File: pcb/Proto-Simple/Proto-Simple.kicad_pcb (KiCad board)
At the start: 2 copper layers, 52 x 63 mm, 339 parts, among them J1 Conn_01x04, J10 Conn_01x01, J11 Conn_01x01, J12 Conn_01x01, J13 Conn_01x01, J14 Conn_01x01, J2 Conn_01x01, J3 Conn_01x01, J4 Conn_01x01, J41 Conn_01x01, J42 Conn_01x01, J43 Conn_01x01, J44 Conn_01x01, J45 Conn_01x01, J46 Conn_01x01, J47 Conn_01x01, J5 Conn_01x01, J6 Conn_01x01, J7 Conn_01x01, J8 Conn_01x01, J9 Conn_01x01, SW100 SW_DPDT_x2, SW101 SW_DPDT_x2

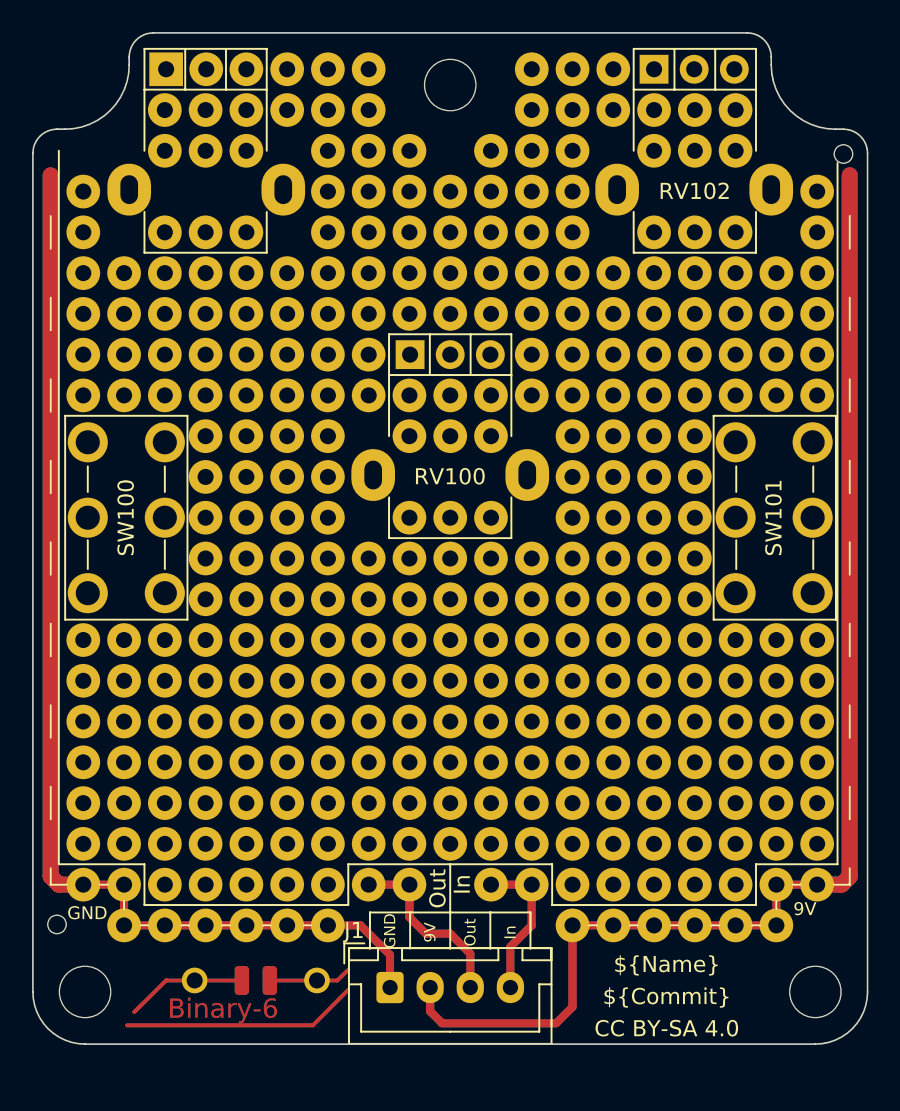
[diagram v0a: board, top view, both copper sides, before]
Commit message: [ProtoSimple] Recreate PCB according to new base template
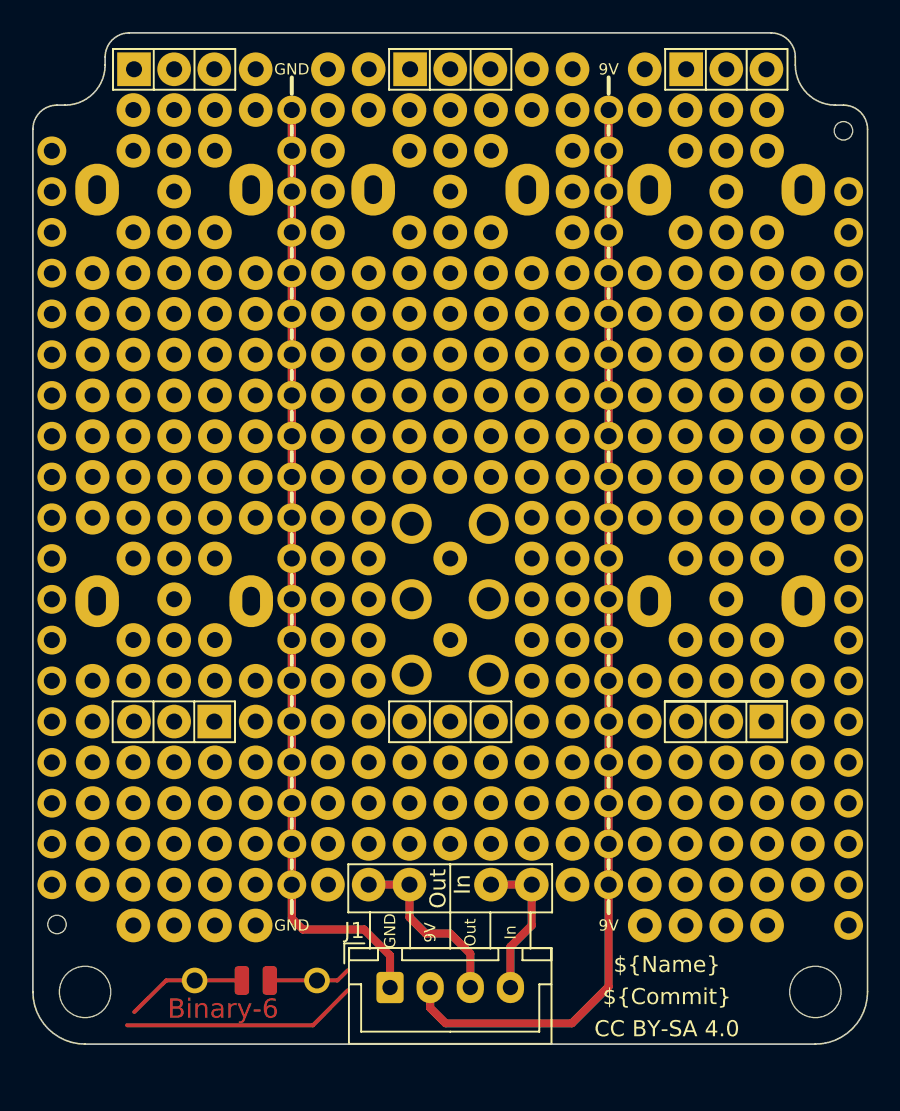
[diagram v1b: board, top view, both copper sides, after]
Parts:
- removed the MK2 at (149.5, 70.8)
- removed the REF** at (162.2, 118.0)
- removed the REF** at (126.6, 87.5)
- removed the REF** at (169.8, 87.5)
- removed the REF** at (134.3, 112.9)
- removed the REF** at (167.3, 120.6)
- removed the REF** at (126.6, 118.0)
- removed the REF** at (134.3, 120.6)
- removed the REF** at (129.2, 105.3)
- removed the REF** at (134.3, 102.8)
- removed the REF** at (149.5, 102.8)
- removed the REF** at (159.7, 120.6)
- removed the REF** at (139.3, 118.0)
- removed the REF** at (147.0, 105.3)
- removed the REF** at (126.6, 90.1)
- removed the REF** at (167.3, 79.9)
- removed the REF** at (129.2, 112.9)
- removed the REF** at (134.3, 100.2)
- removed the REF** at (136.8, 72.3)
- removed the REF** at (131.7, 90.1)
- removed the REF** at (162.2, 107.9)
- removed the REF** at (131.7, 107.9)
- removed the REF** at (164.7, 92.6)
- removed the REF** at (147.0, 97.7)
- removed the REF** at (164.7, 100.2)
- removed the REF** at (139.3, 92.6)
- removed the REF** at (164.7, 90.1)
- removed the REF** at (131.7, 74.8)
- removed the REF** at (167.3, 112.9)
- removed the REF** at (162.2, 87.5)
- removed the REF** at (126.6, 107.9)
- removed the REF** at (134.3, 118.0)
- removed the REF** at (131.7, 118.0)
- removed the REF** at (126.6, 82.5)
- removed the REF** at (172.4, 118.0)
- removed the REF** at (139.3, 85.0)
- removed the REF** at (129.2, 107.9)
- removed the REF** at (159.7, 115.5)
- removed the REF** at (129.2, 90.1)
- removed the REF** at (154.6, 79.9)
- removed the REF** at (136.8, 110.4)
- removed the REF** at (167.3, 118.0)
- removed the REF** at (164.7, 112.9)
- removed the REF** at (162.2, 100.2)
- removed the REF** at (139.3, 72.3)
- removed the REF** at (139.3, 107.9)
- removed the REF** at (164.7, 87.5)
- removed the REF** at (159.7, 69.8)
- removed the REF** at (139.3, 82.5)
- removed the REF** at (162.2, 74.8)
- removed the REF** at (134.3, 90.1)
- removed the REF** at (136.8, 107.9)
- removed the REF** at (126.6, 112.9)
- removed the REF** at (162.2, 90.1)
- removed the REF** at (162.2, 112.9)
- removed the REF** at (162.2, 72.3)
- removed the REF** at (126.6, 110.4)
- removed the REF** at (136.8, 74.8)
- removed the REF** at (159.7, 85.0)
- removed the REF** at (144.4, 74.8)
- removed the REF** at (164.7, 95.2)
- removed the REF** at (134.3, 74.8)
- removed the REF** at (126.6, 115.5)
- removed the REF** at (167.3, 82.5)
- removed the REF** at (139.3, 95.2)
- removed the REF** at (162.2, 120.6)
- removed the REF** at (172.4, 105.3)
- removed the REF** at (172.4, 85.0)
- removed the REF** at (147.0, 102.8)
- removed the REF** at (136.8, 85.0)
- removed the REF** at (159.7, 100.2)
- removed the REF** at (129.2, 87.5)
- removed the REF** at (129.2, 110.4)
- removed the REF** at (164.7, 107.9)
- removed the REF** at (154.6, 74.8)
- removed the REF** at (169.8, 107.9)
- removed the REF** at (136.8, 105.3)
- removed the REF** at (134.3, 79.9)
- removed the REF** at (164.7, 74.8)
- removed the REF** at (136.8, 120.6)
- removed the REF** at (139.3, 102.8)
- removed the REF** at (164.7, 79.9)
- removed the REF** at (134.3, 107.9)
- removed the REF** at (147.0, 100.2)
- removed the REF** at (167.3, 72.3)
- removed the REF** at (159.7, 92.6)
- removed the REF** at (129.2, 115.5)
- removed the REF** at (139.3, 100.2)
- removed the REF** at (131.7, 87.5)
- removed the REF** at (139.3, 115.5)
- removed the REF** at (134.3, 110.4)
- removed the REF** at (139.3, 90.1)
- removed the REF** at (164.7, 105.3)
- removed the REF** at (131.7, 79.9)
- removed the REF** at (159.7, 102.8)
- removed the REF** at (136.8, 97.7)
- removed the REF** at (126.6, 85.0)
- removed the REF** at (169.8, 112.9)
- removed the REF** at (162.2, 102.8)
- removed the REF** at (126.6, 77.4)
- removed the REF** at (159.7, 87.5)
- removed the REF** at (164.7, 118.0)
- removed the REF** at (152.0, 97.7)
- removed the REF** at (147.0, 107.9)
- removed the REF** at (164.7, 115.5)
- removed the REF** at (139.3, 69.8)
- removed the REF** at (136.8, 100.2)
- removed the REF** at (162.2, 79.9)
- removed the REF** at (144.4, 77.4)
- removed the REF** at (169.8, 82.5)
- removed the REF** at (172.4, 110.4)
- removed the REF** at (134.3, 82.5)
- removed the REF** at (152.0, 107.9)
- removed the REF** at (159.7, 105.3)
- removed the REF** at (134.3, 115.5)
- removed the REF** at (139.3, 97.7)
- removed the REF** at (136.8, 95.2)
- removed the REF** at (172.4, 90.1)
- removed the REF** at (169.8, 85.0)
- removed the REF** at (152.0, 100.2)
- removed the REF** at (159.7, 90.1)
- removed the REF** at (169.8, 115.5)
- removed the REF** at (159.7, 82.5)
- removed the REF** at (152.0, 77.4)
- removed the REF** at (129.2, 82.5)
- removed the REF** at (159.7, 118.0)
- removed the REF** at (162.2, 95.2)
- removed the REF** at (172.4, 79.9)
- removed the REF** at (172.4, 82.5)
- removed the REF** at (126.6, 105.3)
- removed the REF** at (172.4, 77.4)
- removed the REF** at (136.8, 112.9)
- removed the REF** at (134.3, 85.0)
- removed the REF** at (131.7, 105.3)
- removed the REF** at (136.8, 82.5)
- removed the REF** at (164.7, 85.0)
- removed the REF** at (136.8, 118.0)
- removed the REF** at (164.7, 120.6)
- removed the REF** at (172.4, 87.5)
- removed the REF** at (136.8, 87.5)
- removed the REF** at (131.7, 72.3)
- removed the REF** at (139.3, 120.6)
- removed the REF** at (162.2, 85.0)
- removed the REF** at (167.3, 87.5)
- removed the REF** at (167.3, 85.0)
- removed the REF** at (162.2, 82.5)
- removed the REF** at (149.5, 97.7)
- removed the REF** at (131.7, 110.4)
- removed the REF** at (152.0, 102.8)
- removed the REF** at (167.3, 107.9)
- removed the REF** at (169.8, 90.1)
- removed the REF** at (139.3, 105.3)
- removed the REF** at (136.8, 115.5)
- removed the REF** at (136.8, 102.8)
- removed the REF** at (136.8, 79.9)
- removed the REF** at (129.2, 118.0)
- removed the REF** at (167.3, 74.8)
- removed the REF** at (136.8, 92.6)
- removed the REF** at (159.7, 107.9)
- removed the REF** at (134.3, 92.6)
- removed the REF** at (164.7, 97.7)
- removed the REF** at (129.2, 85.0)
- removed the REF** at (159.7, 97.7)
- removed the REF** at (159.7, 112.9)
- removed the REF** at (159.7, 72.3)
- removed the REF** at (139.3, 112.9)
- removed the REF** at (149.5, 107.9)
- removed the REF** at (162.2, 97.7)
- removed the REF** at (134.3, 97.7)
- removed the REF** at (164.7, 72.3)
- removed the REF** at (126.6, 79.9)
- removed the REF** at (164.7, 82.5)
- removed the REF** at (139.3, 110.4)
- removed the REF** at (162.2, 105.3)
- removed the REF** at (131.7, 112.9)
- removed the REF** at (139.3, 87.5)
- removed the REF** at (169.8, 105.3)
- removed the REF** at (167.3, 90.1)
- removed the REF** at (159.7, 110.4)
- removed the REF** at (152.0, 105.3)
- removed the REF** at (172.4, 107.9)
- removed the REF** at (131.7, 115.5)
- removed the REF** at (169.8, 110.4)
- removed the REF** at (164.7, 110.4)
- removed the REF** at (167.3, 110.4)
- removed the REF** at (162.2, 110.4)
- removed the REF** at (172.4, 112.9)
- removed the REF** at (134.3, 105.3)
- removed the REF** at (172.4, 115.5)
- removed the REF** at (144.4, 79.9)
- removed the REF** at (154.6, 77.4)
- removed the REF** at (134.3, 72.3)
- removed the REF** at (162.2, 92.6)
- removed the REF** at (167.3, 105.3)
- removed the REF** at (169.8, 118.0)
- removed the REF** at (134.3, 95.2)
- removed the REF** at (162.2, 115.5)
- removed the REF** at (131.7, 82.5)
- removed the REF** at (131.7, 120.6)
- removed the REF** at (134.3, 87.5)
- removed the REF** at (164.7, 102.8)
- removed the REF** at (136.8, 90.1)
- removed the REF** at (167.3, 115.5)
- removed the REF** at (131.7, 85.0)
- removed the REF** at (159.7, 95.2)
- removed the REF** at (147.0, 77.4)
- removed SW100, SW101: SW_DPDT_x2, MeineBib:Switch_toggle_DPDT_Print
- added J15: Conn_01x01, MeineBib:Protopin_Small, F.Cu at (159.4, 112.9)
- added J16: Conn_01x01, MeineBib:Protopin_Small, F.Cu at (159.4, 92.6)
- added J17: Conn_01x01, MeineBib:Protopin_Small, F.Cu at (159.4, 120.6)
- added J18: Conn_01x01, MeineBib:Protopin_Small, F.Cu at (159.4, 110.4)
- added J19: Conn_01x01, MeineBib:Protopin_Small, F.Cu at (159.4, 100.2)
- added J20: Conn_01x01, MeineBib:Protopin_Small, F.Cu at (159.4, 107.9)
- added J21: Conn_01x01, MeineBib:Protopin_Small, F.Cu at (159.4, 74.8)
- added J22: Conn_01x01, MeineBib:Protopin_Small, F.Cu at (159.4, 118.0)
- added J23: Conn_01x01, MeineBib:Protopin_Small, F.Cu at (159.4, 87.5)
- added J24: Conn_01x01, MeineBib:Protopin_Small, F.Cu at (159.4, 102.8)
- added J25: Conn_01x01, MeineBib:Protopin_Small, F.Cu at (159.4, 85.0)
- added J26: Conn_01x01, MeineBib:Protopin_Small, F.Cu at (159.4, 105.3)
- added J27: Conn_01x01, MeineBib:Protopin_Small, F.Cu at (139.6, 100.2)
- added J28: Conn_01x01, MeineBib:Protopin_Small, F.Cu at (139.6, 107.9)
- added J29: Conn_01x01, MeineBib:Protopin_Small, F.Cu at (139.6, 74.8)
- added J30: Conn_01x01, MeineBib:Protopin_Small, F.Cu at (139.6, 90.1)
- added J31: Conn_01x01, MeineBib:Protopin_Small, F.Cu at (139.6, 115.5)
- added J32: Conn_01x01, MeineBib:Protopin_Small, F.Cu at (139.6, 72.3)
- added J33: Conn_01x01, MeineBib:Protopin_Small, F.Cu at (139.6, 87.5)
- added J34: Conn_01x01, MeineBib:Protopin_Small, F.Cu at (139.6, 110.4)
- added J35: Conn_01x01, MeineBib:Protopin_Small, F.Cu at (139.6, 105.3)
- added J36: Conn_01x01, MeineBib:Protopin_Small, F.Cu at (139.6, 77.4)
- added J37: Conn_01x01, MeineBib:Protopin_Small, F.Cu at (139.6, 85.0)
- added J38: Conn_01x01, MeineBib:Protopin_Small, F.Cu at (139.6, 79.9)
- added REF**: Protopin, MeineBib:Protopin, F.Cu at (164.2, 105.3)
- added REF**: Protopin_Small, MeineBib:Protopin_Small, F.Cu at (174.3, 92.6)
- added REF**: Protopin, MeineBib:Protopin, F.Cu at (132.3, 87.5)
- added REF**: Protopin_Small, MeineBib:Protopin_Small, F.Cu at (124.7, 115.5)
- added REF**: Protopin, MeineBib:Protopin, F.Cu at (166.7, 95.2)
- added REF**: Protopin, MeineBib:Protopin, F.Cu at (127.2, 107.9)
- added REF**: Protopin, MeineBib:Protopin, F.Cu at (134.8, 97.7)
- added REF**: Protopin, MeineBib:Protopin, F.Cu at (127.2, 110.4)
- added REF**: Protopin_Small, MeineBib:Protopin_Small, F.Cu at (124.7, 110.4)
- added REF**: Protopin, MeineBib:Protopin, F.Cu at (132.3, 97.7)
- added REF**: Protopin, MeineBib:Protopin, F.Cu at (137.4, 107.9)
- added REF**: Protopin, MeineBib:Protopin, F.Cu at (127.2, 92.6)
- added REF**: Protopin, MeineBib:Protopin, F.Cu at (129.8, 112.9)
- added REF**: Protopin, MeineBib:Protopin, F.Cu at (129.8, 97.7)
- added REF**: Protopin_Small, MeineBib:Protopin_Small, F.Cu at (174.3, 77.4)
- added REF**: Protopin, MeineBib:Protopin, F.Cu at (137.4, 115.5)
- added REF**: Protopin_Small, MeineBib:Protopin_Small, F.Cu at (174.3, 97.7)
- added REF**: Protopin, MeineBib:Protopin, F.Cu at (161.6, 90.1)
- added REF**: Protopin, MeineBib:Protopin, F.Cu at (134.8, 82.5)
- added REF**: Protopin, MeineBib:Protopin, F.Cu at (171.8, 85.0)
- added REF**: Protopin, MeineBib:Protopin, F.Cu at (134.8, 112.9)
- added REF**: Protopin, MeineBib:Protopin, F.Cu at (137.4, 85.0)
- added REF**: Protopin, MeineBib:Protopin, F.Cu at (132.3, 105.3)
- added REF**: Protopin, MeineBib:Protopin, F.Cu at (129.8, 85.0)
- added REF**: Protopin, MeineBib:Protopin, F.Cu at (129.8, 79.9)
- added REF**: Protopin, MeineBib:Protopin, F.Cu at (132.3, 95.2)
- added REF**: Protopin, MeineBib:Protopin, F.Cu at (129.8, 95.2)
- added REF**: Protopin_Small, MeineBib:Protopin_Small, F.Cu at (124.7, 77.4)
- added REF**: Protopin, MeineBib:Protopin, F.Cu at (134.8, 79.9)
- added REF**: Protopin, MeineBib:Protopin, F.Cu at (166.7, 107.9)
- added REF**: Protopin, MeineBib:Protopin, F.Cu at (164.2, 112.9)
- added REF**: Protopin, MeineBib:Protopin, F.Cu at (132.3, 102.8)
- added REF**: Protopin, MeineBib:Protopin, F.Cu at (132.3, 90.1)
- added REF**: Protopin, MeineBib:Protopin, F.Cu at (161.6, 97.7)
- added REF**: Protopin_Small, MeineBib:Protopin_Small, F.Cu at (174.3, 110.4)
- added REF**: Protopin, MeineBib:Protopin, F.Cu at (161.6, 95.2)
- added REF**: Protopin, MeineBib:Protopin, F.Cu at (134.8, 115.5)
- added REF**: Protopin_Small, MeineBib:Protopin_Small, F.Cu at (124.7, 95.2)
- added REF**: Protopin, MeineBib:Protopin, F.Cu at (166.7, 72.3)
- added REF**: Protopin, MeineBib:Protopin, F.Cu at (171.8, 115.5)
- added REF**: Protopin, MeineBib:Protopin, F.Cu at (161.6, 107.9)
- added REF**: Protopin, MeineBib:Protopin, F.Cu at (166.7, 92.6)
- added REF**: Protopin_Small, MeineBib:Protopin_Small, F.Cu at (124.7, 105.3)
- added REF**: Protopin, MeineBib:Protopin, F.Cu at (169.2, 95.2)
- added REF**: Protopin, MeineBib:Protopin, F.Cu at (169.2, 79.9)
- added REF**: Protopin, MeineBib:Protopin, F.Cu at (169.2, 100.2)
- added REF**: Protopin, MeineBib:Protopin, F.Cu at (132.3, 79.9)
- added REF**: Protopin_Small, MeineBib:Protopin_Small, F.Cu at (174.3, 105.3)
- added REF**: Protopin, MeineBib:Protopin, F.Cu at (134.8, 123.1)
- added REF**: Protopin, MeineBib:Protopin, F.Cu at (169.2, 112.9)
- added REF**: Protopin_Small, MeineBib:Protopin_Small, F.Cu at (174.3, 90.1)
- added REF**: Protopin, MeineBib:Protopin, F.Cu at (129.8, 82.5)
- added REF**: Protopin_Small, MeineBib:Protopin_Small, F.Cu at (124.7, 82.5)
- added REF**: Protopin, MeineBib:Protopin, F.Cu at (166.7, 77.4)
- added REF**: Protopin, MeineBib:Protopin, F.Cu at (129.8, 118.0)
- added REF**: Protopin, MeineBib:Protopin, F.Cu at (164.2, 90.1)
- added REF**: Protopin, MeineBib:Protopin, F.Cu at (161.6, 112.9)
- added REF**: Protopin, MeineBib:Protopin, F.Cu at (164.2, 74.8)
- added REF**: Protopin, MeineBib:Protopin, F.Cu at (132.3, 107.9)
- added REF**: Protopin_Small, MeineBib:Protopin_Small, F.Cu at (124.7, 120.6)
- added REF**: Protopin, MeineBib:Protopin, F.Cu at (132.3, 92.6)
- added REF**: Protopin, MeineBib:Protopin, F.Cu at (161.6, 118.0)
- added REF**: Protopin, MeineBib:Protopin, F.Cu at (129.8, 115.5)
- added REF**: Protopin, MeineBib:Protopin, F.Cu at (164.2, 100.2)
- added REF**: Protopin, MeineBib:Protopin, F.Cu at (134.8, 90.1)
- added REF**: Protopin, MeineBib:Protopin, F.Cu at (169.2, 72.3)
- added REF**: Protopin, MeineBib:Protopin, F.Cu at (132.3, 100.2)
- added REF**: Protopin, MeineBib:Protopin, F.Cu at (166.7, 85.0)
- added REF**: Protopin, MeineBib:Protopin, F.Cu at (132.3, 115.5)
- added REF**: Protopin, MeineBib:Protopin, F.Cu at (127.2, 112.9)
- added REF**: Protopin_Small, MeineBib:Protopin_Small, F.Cu at (124.7, 118.0)
- added REF**: Protopin, MeineBib:Protopin, F.Cu at (129.8, 74.8)
- added REF**: Protopin, MeineBib:Protopin, F.Cu at (134.8, 100.2)
- added REF**: Protopin, MeineBib:Protopin, F.Cu at (161.6, 92.6)
- added REF**: Protopin, MeineBib:Protopin, F.Cu at (166.7, 87.5)
- added REF**: Protopin, MeineBib:Protopin, F.Cu at (134.8, 95.2)
- added REF**: Protopin, MeineBib:Protopin, F.Cu at (166.7, 97.7)
- added REF**: Protopin, MeineBib:Protopin, F.Cu at (132.3, 72.3)
- added REF**: Protopin, MeineBib:Protopin, F.Cu at (161.6, 87.5)
- added REF**: Protopin, MeineBib:Protopin, F.Cu at (171.8, 110.4)
- added REF**: Protopin, MeineBib:Protopin, F.Cu at (144.4, 97.7)
- added REF**: Protopin, MeineBib:Protopin, F.Cu at (137.4, 92.6)
- added REF**: Protopin_Small, MeineBib:Protopin_Small, F.Cu at (174.3, 100.2)
- added REF**: Protopin, MeineBib:Protopin, F.Cu at (166.7, 100.2)
- added REF**: Protopin, MeineBib:Protopin, F.Cu at (161.6, 120.6)
- added REF**: Protopin, MeineBib:Protopin, F.Cu at (164.2, 79.9)
- added REF**: Protopin_Small, MeineBib:Protopin_Small, F.Cu at (124.7, 90.1)
- added REF**: Protopin, MeineBib:Protopin, F.Cu at (132.3, 85.0)
- added REF**: Protopin, MeineBib:Protopin, F.Cu at (137.4, 112.9)
- added REF**: Protopin, MeineBib:Protopin, F.Cu at (166.7, 118.0)
- added REF**: Protopin, MeineBib:Protopin, F.Cu at (149.5, 72.3)
- added REF**: Protopin, MeineBib:Protopin, F.Cu at (129.8, 107.9)
- added REF**: Protopin, MeineBib:Protopin, F.Cu at (166.7, 74.8)
- added REF**: Protopin, MeineBib:Protopin, F.Cu at (134.8, 87.5)
- added REF**: Protopin, MeineBib:Protopin, F.Cu at (166.7, 115.5)
- added REF**: Protopin, MeineBib:Protopin, F.Cu at (164.2, 115.5)
- added REF**: Protopin, MeineBib:Protopin, F.Cu at (164.2, 118.0)
- added REF**: Protopin, MeineBib:Protopin, F.Cu at (169.2, 120.6)
- added REF**: Protopin_Small, MeineBib:Protopin_Small, F.Cu at (124.7, 107.9)
- added REF**: Protopin, MeineBib:Protopin, F.Cu at (129.8, 72.3)
- added REF**: Protopin, MeineBib:Protopin, F.Cu at (137.4, 110.4)
- added REF**: Protopin_Small, MeineBib:Protopin_Small, F.Cu at (174.3, 87.5)
- added REF**: Protopin, MeineBib:Protopin, F.Cu at (134.8, 85.0)
- added REF**: Protopin, MeineBib:Protopin, F.Cu at (137.4, 69.8)
- added REF**: Protopin, MeineBib:Protopin, F.Cu at (171.8, 95.2)
- added REF**: Protopin, MeineBib:Protopin, F.Cu at (152.0, 95.2)
- added REF**: Protopin, MeineBib:Protopin, F.Cu at (166.7, 82.5)
- added REF**: Protopin, MeineBib:Protopin, F.Cu at (129.8, 92.6)
- added REF**: Protopin_Small, MeineBib:Protopin_Small, F.Cu at (174.3, 79.9)
- added REF**: Protopin, MeineBib:Protopin, F.Cu at (129.8, 87.5)
- added REF**: Protopin, MeineBib:Protopin, F.Cu at (147.0, 72.3)
- added REF**: Protopin, MeineBib:Protopin, F.Cu at (137.4, 82.5)
- added REF**: Protopin, MeineBib:Protopin, F.Cu at (171.8, 92.6)
- added REF**: Protopin, MeineBib:Protopin, F.Cu at (154.6, 92.6)
- added REF**: Protopin, MeineBib:Protopin, F.Cu at (137.4, 90.1)
- added REF**: Protopin_Small, MeineBib:Protopin_Small, F.Cu at (174.3, 120.6)
- added REF**: Protopin, MeineBib:Protopin, F.Cu at (171.8, 120.6)
- added REF**: Protopin, MeineBib:Protopin, F.Cu at (127.2, 95.2)
- added REF**: Protopin, MeineBib:Protopin, F.Cu at (161.6, 69.8)
- added REF**: Protopin_Small, MeineBib:Protopin_Small, F.Cu at (174.3, 115.5)
- added REF**: Protopin, MeineBib:Protopin, F.Cu at (134.8, 72.3)
- added REF**: Protopin, MeineBib:Protopin, F.Cu at (161.6, 85.0)
- added REF**: Protopin, MeineBib:Protopin, F.Cu at (132.3, 77.4)
- added REF**: Protopin, MeineBib:Protopin, F.Cu at (169.2, 90.1)
- added REF**: Protopin, MeineBib:Protopin, F.Cu at (161.6, 115.5)
- added REF**: Protopin, MeineBib:Protopin, F.Cu at (164.2, 97.7)
- added REF**: Protopin_Small, MeineBib:Protopin_Small, F.Cu at (174.3, 95.2)
- added REF**: Protopin_Small, MeineBib:Protopin_Small, F.Cu at (174.3, 85.0)
- added REF**: Protopin, MeineBib:Protopin, F.Cu at (132.3, 74.8)
- added REF**: Protopin, MeineBib:Protopin, F.Cu at (169.2, 92.6)
- added REF**: Protopin_Small, MeineBib:Protopin_Small, F.Cu at (174.3, 102.8)
- added REF**: Protopin, MeineBib:Protopin, F.Cu at (164.2, 92.6)
- added REF**: Protopin, MeineBib:Protopin, F.Cu at (132.3, 120.6)
- added REF**: Protopin, MeineBib:Protopin, F.Cu at (137.4, 123.1)
- added REF**: Protopin, MeineBib:Protopin, F.Cu at (149.5, 87.5)
- added REF**: Protopin, MeineBib:Protopin, F.Cu at (137.4, 120.6)
- added REF**: Protopin_Small, MeineBib:Protopin_Small, F.Cu at (174.3, 113.0)
- added REF**: Protopin, MeineBib:Protopin, F.Cu at (132.3, 123.1)
- added REF**: Protopin, MeineBib:Protopin, F.Cu at (154.6, 95.2)
- added REF**: Protopin_Small, MeineBib:Protopin_Small, F.Cu at (124.7, 113.0)
- added REF**: Protopin, MeineBib:Protopin, F.Cu at (171.8, 118.0)
- added REF**: Protopin_Small, MeineBib:Protopin_Small, F.Cu at (124.7, 102.8)
- added REF**: Protopin, MeineBib:Protopin, F.Cu at (164.2, 87.5)
- added REF**: Protopin, MeineBib:Protopin, F.Cu at (169.2, 123.1)
- added REF**: Protopin, MeineBib:Protopin, F.Cu at (129.8, 90.1)
- added REF**: Protopin, MeineBib:Protopin, F.Cu at (164.2, 85.0)
- added REF**: Protopin, MeineBib:Protopin, F.Cu at (169.2, 97.7)
- added REF**: Protopin, MeineBib:Protopin, F.Cu at (166.7, 120.6)
- added REF**: Protopin, MeineBib:Protopin, F.Cu at (164.2, 95.2)
- added REF**: Protopin, MeineBib:Protopin, F.Cu at (149.5, 74.8)
- added REF**: Protopin_Small, MeineBib:Protopin_Small, F.Cu at (124.7, 85.0)
- added REF**: Protopin, MeineBib:Protopin, F.Cu at (152.0, 87.5)
- added REF**: Protopin, MeineBib:Protopin, F.Cu at (127.2, 115.5)
- added REF**: Protopin_Small, MeineBib:Protopin_Small, F.Cu at (124.7, 87.5)
- added REF**: Protopin, MeineBib:Protopin, F.Cu at (137.4, 95.2)
- added REF**: Protopin, MeineBib:Protopin, F.Cu at (144.4, 92.6)
- added REF**: Protopin, MeineBib:Protopin, F.Cu at (166.7, 123.1)
- added REF**: Protopin, MeineBib:Protopin, F.Cu at (166.7, 90.1)
- added REF**: Protopin, MeineBib:Protopin, F.Cu at (134.8, 92.6)
- added REF**: Protopin, MeineBib:Protopin, F.Cu at (161.6, 110.4)
- added REF**: Protopin, MeineBib:Protopin, F.Cu at (164.2, 82.5)
- added REF**: Protopin, MeineBib:Protopin, F.Cu at (137.4, 72.3)
- added REF**: Protopin, MeineBib:Protopin, F.Cu at (169.2, 87.5)
- added REF**: Protopin, MeineBib:Protopin, F.Cu at (161.6, 72.3)
- added REF**: Protopin, MeineBib:Protopin, F.Cu at (127.2, 97.7)
- added REF**: Protopin, MeineBib:Protopin, F.Cu at (164.2, 107.9)
- added REF**: Protopin, MeineBib:Protopin, F.Cu at (129.8, 100.2)
- added REF**: Protopin, MeineBib:Protopin, F.Cu at (164.2, 72.3)
- added REF**: Protopin, MeineBib:Protopin, F.Cu at (166.7, 102.8)
- added REF**: Protopin, MeineBib:Protopin, F.Cu at (147.0, 87.5)
- added REF**: Protopin, MeineBib:Protopin, F.Cu at (127.2, 118.0)
- added REF**: Protopin, MeineBib:Protopin, F.Cu at (171.8, 87.5)
- added REF**: Protopin_Small, MeineBib:Protopin_Small, F.Cu at (124.7, 97.7)
- added REF**: Protopin_Small, MeineBib:Protopin_Small, F.Cu at (124.7, 92.6)
- added REF**: OSHW-Symbol_6.7x6mm_SilkScreen, Symbol:OSHW-Symbol_6.7x6mm_SilkScreen, B.Cu at (137.4, 127.4)
- added REF**: Switch_toggle_DPDT_Print, MeineBib:Switch_toggle_DPDT_Print, B.Cu at (149.5, 102.8)
- added REF**: Protopin_Small, MeineBib:Protopin_Small, F.Cu at (124.7, 74.8)
- added REF**: Protopin, MeineBib:Protopin, F.Cu at (134.8, 118.0)
- added REF**: Protopin, MeineBib:Protopin, F.Cu at (169.2, 118.0)
- added REF**: Protopin, MeineBib:Protopin, F.Cu at (171.8, 107.9)
- added REF**: Protopin, MeineBib:Protopin, F.Cu at (169.2, 74.8)
- added REF**: Protopin, MeineBib:Protopin, F.Cu at (134.8, 107.9)
- added REF**: Protopin, MeineBib:Protopin, F.Cu at (127.2, 120.6)
- added REF**: Protopin, MeineBib:Protopin, F.Cu at (171.8, 97.7)
- added REF**: Protopin, MeineBib:Protopin, F.Cu at (171.8, 112.9)
- added REF**: Protopin, MeineBib:Protopin, F.Cu at (161.6, 82.5)
- added REF**: Protopin, MeineBib:Protopin, F.Cu at (164.2, 120.6)
- added REF**: Protopin, MeineBib:Protopin, F.Cu at (137.4, 97.7)
- added REF**: Protopin, MeineBib:Protopin, F.Cu at (134.8, 120.6)
- added REF**: Protopin_Small, MeineBib:Protopin_Small, F.Cu at (174.3, 82.5)
- added REF**: Protopin, MeineBib:Protopin, F.Cu at (169.2, 107.9)
- added REF**: Protopin, MeineBib:Protopin, F.Cu at (144.4, 95.2)
- added REF**: Protopin, MeineBib:Protopin, F.Cu at (127.2, 87.5)
- added REF**: Protopin, MeineBib:Protopin, F.Cu at (132.3, 118.0)
- added REF**: Protopin_Small, MeineBib:Protopin_Small, F.Cu at (124.7, 79.9)
- added REF**: Protopin_Small, MeineBib:Protopin_Small, F.Cu at (174.3, 107.9)
- added REF**: Protopin_Small, MeineBib:Protopin_Small, F.Cu at (174.3, 118.0)
- added REF**: Protopin, MeineBib:Protopin, F.Cu at (129.8, 123.1)
- added REF**: Protopin, MeineBib:Protopin, F.Cu at (154.6, 97.7)
- added REF**: Protopin, MeineBib:Protopin, F.Cu at (171.8, 90.1)
- added REF**: Protopin, MeineBib:Protopin, F.Cu at (132.3, 112.9)
- added REF**: Protopin, MeineBib:Protopin, F.Cu at (132.3, 82.5)
- added REF**: Protopin, MeineBib:Protopin, F.Cu at (127.2, 90.1)
- added REF**: Protopin, MeineBib:Protopin, F.Cu at (164.2, 123.1)
- added REF**: Protopin, MeineBib:Protopin, F.Cu at (169.2, 105.3)
- added REF**: Protopin, MeineBib:Protopin, F.Cu at (134.8, 105.3)
- added REF**: Protopin, MeineBib:Protopin, F.Cu at (169.2, 115.5)
- added REF**: Protopin, MeineBib:Protopin, F.Cu at (171.8, 82.5)
- added REF**: Protopin, MeineBib:Protopin, F.Cu at (166.7, 79.9)
- added REF**: Protopin, MeineBib:Protopin, F.Cu at (127.2, 85.0)
- added REF**: Protopin, MeineBib:Protopin, F.Cu at (137.4, 118.0)
- added REF**: Protopin_Small, MeineBib:Protopin_Small, F.Cu at (124.7, 100.2)
- added REF**: Protopin, MeineBib:Protopin, F.Cu at (161.6, 123.1)
- added REF**: Protopin, MeineBib:Protopin, F.Cu at (147.0, 95.2)
- added REF**: Protopin, MeineBib:Protopin, F.Cu at (169.2, 85.0)
- added REF**: Protopin, MeineBib:Protopin, F.Cu at (149.5, 95.2)
- added REF**: Protopin, MeineBib:Protopin, F.Cu at (134.8, 74.8)
- added REF**: Protopin, MeineBib:Protopin, F.Cu at (129.8, 120.6)
- added REF**: Protopin, MeineBib:Protopin, F.Cu at (166.7, 105.3)
- added REF**: Protopin_Small, MeineBib:Protopin_Small, F.Cu at (174.3, 123.1)
- added REF**: Protopin, MeineBib:Protopin, F.Cu at (129.8, 105.3)
- added REF**: Protopin, MeineBib:Protopin, F.Cu at (169.2, 82.5)
- added REF**: Protopin, MeineBib:Protopin, F.Cu at (137.4, 87.5)
- added REF**: Protopin, MeineBib:Protopin, F.Cu at (152.0, 72.3)
- added REF**: Protopin, MeineBib:Protopin, F.Cu at (166.7, 112.9)
- added REF**: Protopin, MeineBib:Protopin, F.Cu at (127.2, 82.5)
- added RV200: 100K Lin, MeineBib:Potentiometer_Alpha_RD901F-40-00D_Single_Vertical, B.Cu at (134.8, 110.4)
- added RV200: 100K Lin, MeineBib:Potentiometer_Alpha_RD901F-40-00D_Single_Vertical, B.Cu at (169.2, 110.4)
- J10, J11, J12, J13, J14, J41, J42, J43, J44, J45, J46, J47, J6, J7, J8, J9: footprint MeineBib:Protopin -> MeineBib:Protopin_Small
- RV100, RV102: footprint Potentiometer_THT:Potentiometer_Alpha_RD901F-40-00D_Single_Vertical -> MeineBib:Potentiometer_Alpha_RD901F-40-00D_Single_Vertical
- moved J7 50.9 mm to (159.4, 72.3)
- moved J8 45.7 mm to (159.4, 77.4)
- moved J11 43.5 mm to (159.4, 79.9)
- moved J45 42.0 mm to (139.6, 82.5)
- moved J13 41.4 mm to (159.4, 82.5)
- moved J12 33.1 mm to (159.4, 90.1)
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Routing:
- net +9V: track 159.7 -> 136.7 mm
- net GND: track 140.7 -> 118.9 mm
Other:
- outline, holes or cut-outs redrawn

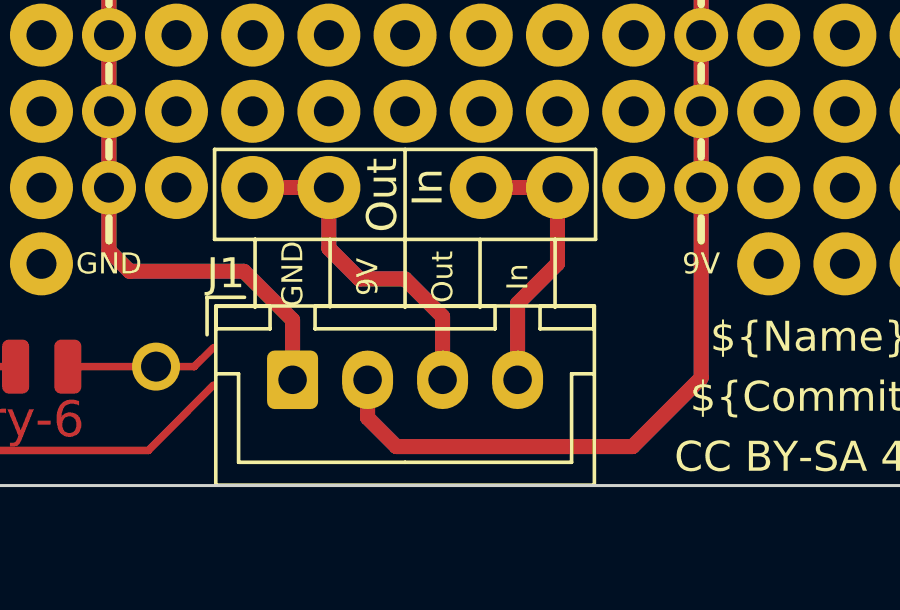
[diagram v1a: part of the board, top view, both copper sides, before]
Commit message: [All] Flip board to board connector on upper PCB (obstructed some silk)
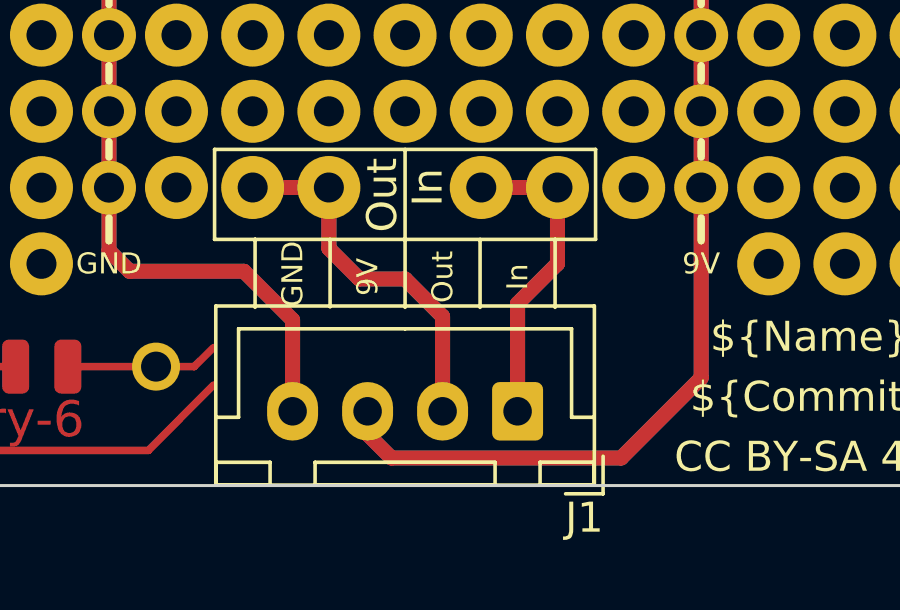
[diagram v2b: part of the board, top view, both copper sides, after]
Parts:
- moved J1 7.57 mm to (153.2, 128.0), turned to 180 degrees
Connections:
- J1 pad 1: GND -> Upper_PCB_Input
- J1 pad 2: +9V -> Upper_PCB_Output
- J1 pad 3: Upper_PCB_Output -> +9V
- J1 pad 4: Upper_PCB_Input -> GND
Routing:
- net Upper_PCB_Output: track 22.8 -> 24.9 mm
- net Upper_PCB_Input: track 19.0 -> 21.1 mm
- net GND: track 118.9 -> 121.0 mm
- net +9V: track 136.7 -> 135.8 mm
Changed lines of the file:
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@@
   )
   (footprint "Connector_JST:JST_XH_B4B-XH-A_1x04_P2.50mm_Vertical" (layer "F.Cu")
-    (at 145.75 126.975)
+    (at 153.25 128.025 180)
     (descr "JST XH series connector, B4B-XH-A (http://www.jst-mfg.com/product/pdf/eng/eXH.pdf), generated with kicad-footprint-generator")
     (tags "connector JST XH vertical")
@@
     (fp_line (start 0 -1.35) (end 0.625 -2.35) (layer "F.Fab") (width 0.1))
     (fp_line (start -2.45 3.4) (end 9.95 3.4) (layer "F.Fab") (width 0.1))
-    (pad "1" thru_hole roundrect (at 0 0) (size 1.7 1.95) (drill 0.95) (layers *.Cu *.Mask) (roundrect_rratio 0.1470588235)
-      (net 2 "GND") (pinfunction "Pin_1") (pintype "passive"))
-    (pad "2" thru_hole oval (at 2.5 0) (size 1.7 1.95) (drill 0.95) (layers *.Cu *.Mask)
-      (net 1 "+9V") (pinfunction "Pin_2") (pintype "passive"))
-    (pad "3" thru_hole oval (at 5 0) (size 1.7 1.95) (drill 0.95) (layers *.Cu *.Mask)
-      (net 4 "Upper_PCB_Output") (pinfunction "Pin_3") (pintype "passive"))
-    (pad "4" thru_hole oval (at 7.5 0) (size 1.7 1.95) (drill 0.95) (layers *.Cu *.Mask)
-      (net 3 "Upper_PCB_Input") (pinfunction "Pin_4") (pintype "passive"))
+    (pad "1" thru_hole roundrect (at 0 0 180) (size 1.7 1.95) (drill 0.95) (layers *.Cu *.Mask) (roundrect_rratio 0.1470588235)
+      (net 3 "Upper_PCB_Input") (pinfunction "Pin_1") (pintype "passive"))
+    (pad "2" thru_hole oval (at 2.5 0 180) (size 1.7 1.95) (drill 0.95) (layers *.Cu *.Mask)
+      (net 4 "Upper_PCB_Output") (pinfunction "Pin_2") (pintype "passive"))
+    (pad "3" thru_hole oval (at 5 0 180) (size 1.7 1.95) (drill 0.95) (layers *.Cu *.Mask)
+      (net 1 "+9V") (pinfunction "Pin_3") (pintype "passive"))
+    (pad "4" thru_hole oval (at 7.5 0 180) (size 1.7 1.95) (drill 0.95) (layers *.Cu *.Mask)
+      (net 2 "GND") (pinfunction "Pin_4") (pintype "passive"))
     (model "${KICAD6_3DMODEL_DIR}/Connector_JST.3dshapes/JST_XH_B4B-XH-A_1x04_P2.50mm_Vertical.wrl"
       (offset (xyz 0 0 0))
@@
   (segment (start 159.37 110.405) (end 159.37 107.865) (width 0.5) (layer "F.Cu") (net 1))
   (segment (start 159.37 100.245) (end 159.37 97.705) (width 0.5) (layer "F.Cu") (net 1))
-  (segment (start 159.37 120.565) (end 159.37 126.915) (width 0.5) (layer "F.Cu") (net 1))
+  (segment (start 149.047 129.582) (end 156.703 129.582) (width 0.5) (layer "F.Cu") (net 1))
   (segment (start 159.37 115.485) (end 159.37 112.945) (width 0.5) (layer "F.Cu") (net 1))
+  (segment (start 148.25 128.025) (end 148.25 128.785) (width 0.5) (layer "F.Cu") (net 1))
   (segment (start 159.37 112.945) (end 159.37 110.405) (width 0.5) (layer "F.Cu") (net 1))
-  (segment (start 157.084 129.201) (end 149.21 129.201) (width 0.5) (layer "F.Cu") (net 1))
   (segment (start 159.37 92.625) (end 159.37 90.085) (width 0.5) (layer "F.Cu") (net 1))
+  (segment (start 148.25 128.785) (end 149.047 129.582) (width 0.5) (layer "F.Cu") (net 1))
   (segment (start 159.37 95.165) (end 159.37 92.625) (width 0.5) (layer "F.Cu") (net 1))
   (segment (start 159.37 82.465) (end 159.37 79.925) (width 0.5) (layer "F.Cu") (net 1))
-  (segment (start 149.21 129.201) (end 148.25 128.241) (width 0.5) (layer "F.Cu") (net 1))
+  (segment (start 156.703 129.582) (end 159.37 126.915) (width 0.5) (layer "F.Cu") (net 1))
   (segment (start 159.37 105.325) (end 159.37 102.785) (width 0.5) (layer "F.Cu") (net 1))
   (segment (start 159.37 97.705) (end 159.37 95.165) (width 0.5) (layer "F.Cu") (net 1))
-  (segment (start 159.37 126.915) (end 157.084 129.201) (width 0.5) (layer "F.Cu") (net 1))
   (segment (start 159.37 102.785) (end 159.37 100.245) (width 0.5) (layer "F.Cu") (net 1))
-  (segment (start 148.25 128.241) (end 148.25 126.975) (width 0.5) (layer "F.Cu") (net 1))
+  (segment (start 159.37 126.915) (end 159.37 120.565) (width 0.5) (layer "F.Cu") (net 1))
   (segment (start 159.37 87.545) (end 159.37 85.005) (width 0.5) (layer "F.Cu") (net 1))
   (segment (start 159.37 107.865) (end 159.37 105.325) (width 0.5) (layer "F.Cu") (net 1))
@@
   (segment (start 159.37 79.925) (end 159.37 77.385) (width 0.5) (layer "F.Cu") (net 1))
   (segment (start 159.37 120.565) (end 159.37 72.305) (width 0.5) (layer "B.Cu") (net 1))
-  (segment (start 149.21 129.201) (end 157.084 129.201) (width 0.5) (layer "B.Cu") (net 1))
   (segment (start 159.37 126.915) (end 159.37 120.565) (width 0.5) (layer "B.Cu") (net 1))
-  (segment (start 148.25 126.975) (end 148.25 128.241) (width 0.5) (layer "B.Cu") (net 1))
-  (segment (start 148.25 128.241) (end 149.21 129.201) (width 0.5) (layer "B.Cu") (net 1))
-  (segment (start 157.084 129.201) (end 159.37 126.915) (width 0.5) (layer "B.Cu") (net 1))
+  (segment (start 148.25 128.025) (end 148.25 128.785) (width 0.5) (layer "B.Cu") (net 1))
+  (segment (start 156.703 129.582) (end 159.37 126.915) (width 0.5) (layer "B.Cu") (net 1))
+  (segment (start 148.25 128.785) (end 149.047 129.582) (width 0.5) (layer "B.Cu") (net 1))
+  (segment (start 149.047 129.582) (end 156.703 129.582) (width 0.5) (layer "B.Cu") (net 1))
   (segment (start 139.63 122.669) (end 139.63 120.57) (width 0.5) (layer "F.Cu") (net 2))
   (segment (start 139.63 82.465) (end 139.63 120.57) (width 0.5) (layer "F.Cu") (net 2))
@@
   (segment (start 139.63 79.925) (end 139.63 82.465) (width 0.5) (layer "F.Cu") (net 2))
   (segment (start 139.63 77.385) (end 139.63 79.925) (width 0.5) (layer "F.Cu") (net 2))
-  (segment (start 145.75 126.975) (end 145.75 124.979) (width 0.5) (layer "F.Cu") (net 2))
+  (segment (start 145.75 124.979) (end 145.75 128.025) (width 0.5) (layer "F.Cu") (net 2))
   (segment (start 140.32 123.359) (end 139.63 122.669) (width 0.5) (layer "F.Cu") (net 2))
   (segment (start 139.63 74.845) (end 139.63 77.385) (width 0.5) (layer "F.Cu") (net 2))
   (segment (start 144.13 123.359) (end 145.75 124.979) (width 0.5) (layer "B.Cu") (net 2))
   (segment (start 139.63 122.669) (end 140.32 123.359) (width 0.5) (layer "B.Cu") (net 2))
-  (segment (start 145.75 124.979) (end 145.75 126.975) (width 0.5) (layer "B.Cu") (net 2))
   (segment (start 140.32 123.359) (end 144.13 123.359) (width 0.5) (layer "B.Cu") (net 2))
+  (segment (start 145.75 124.979) (end 145.75 128.025) (width 0.5) (layer "B.Cu") (net 2))
   (segment (start 139.63 120.57) (end 139.63 122.669) (width 0.5) (layer "B.Cu") (net 2))
   (segment (start 139.63 72.305) (end 139.63 120.57) (width 0.5) (layer "B.Cu") (net 2))
   (segment (start 154.58 120.565) (end 152.04 120.565) (width 0.5) (layer "F.Cu") (net 3))
-  (segment (start 153.25 126.975) (end 153.25 124.435) (width 0.5) (layer "F.Cu") (net 3))
   (segment (start 154.58 123.105) (end 154.58 120.565) (width 0.5) (layer "F.Cu") (net 3))
+  (segment (start 153.25 124.435) (end 153.25 128.025) (width 0.5) (layer "F.Cu") (net 3))
   (segment (start 153.25 124.435) (end 154.58 123.105) (width 0.5) (layer "F.Cu") (net 3))
   (segment (start 154.58 123.105) (end 154.58 120.565) (width 0.5) (layer "B.Cu") (net 3))
+  (segment (start 153.25 124.435) (end 153.25 128.025) (width 0.5) (layer "B.Cu") (net 3))
   (segment (start 154.58 120.565) (end 152.04 120.565) (width 0.5) (layer "B.Cu") (net 3))
   (segment (start 153.25 124.435) (end 154.58 123.105) (width 0.5) (layer "B.Cu") (net 3))
-  (segment (start 153.25 126.975) (end 153.25 124.435) (width 0.5) (layer "B.Cu") (net 3))
   (segment (start 146.96 122.597) (end 147.976 123.613) (width 0.5) (layer "F.Cu") (net 4))
-  (segment (start 150.75 124.863) (end 150.75 126.975) (width 0.5) (layer "F.Cu") (net 4))
   (segment (start 149.5 123.613) (end 150.75 124.863) (width 0.5) (layer "F.Cu") (net 4))
+  (segment (start 150.75 124.863) (end 150.75 128.025) (width 0.5) (layer "F.Cu") (net 4))
   (segment (start 146.96 120.565) (end 146.96 122.597) (width 0.5) (layer "F.Cu") (net 4))
   (segment (start 144.42 120.565) (end 146.96 120.565) (width 0.5) (layer "F.Cu") (net 4))
@@
   (segment (start 149.5 123.613) (end 147.976 123.613) (width 0.5) (layer "B.Cu") (net 4))
   (segment (start 146.96 122.597) (end 146.96 120.565) (width 0.5) (layer "B.Cu") (net 4))
+  (segment (start 150.75 124.863) (end 150.75 128.025) (width 0.5) (layer "B.Cu") (net 4))
   (segment (start 147.976 123.613) (end 146.96 122.597) (width 0.5) (layer "B.Cu") (net 4))
-  (segment (start 150.75 126.975) (end 150.75 124.863) (width 0.5) (layer "B.Cu") (net 4))
 )
